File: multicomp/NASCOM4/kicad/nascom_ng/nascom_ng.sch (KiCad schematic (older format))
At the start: 20 parts, among them J1 Conn_02x14_Even_Odd, J14 Conn_02x08_Odd_Even, J2 Conn_02x14_Even_Odd, J3 Conn_02x14_Even_Odd, J4 Conn_02x14_Even_Odd, SW1 SW_Push, SW2 SW_Push, SW3 SW_Push

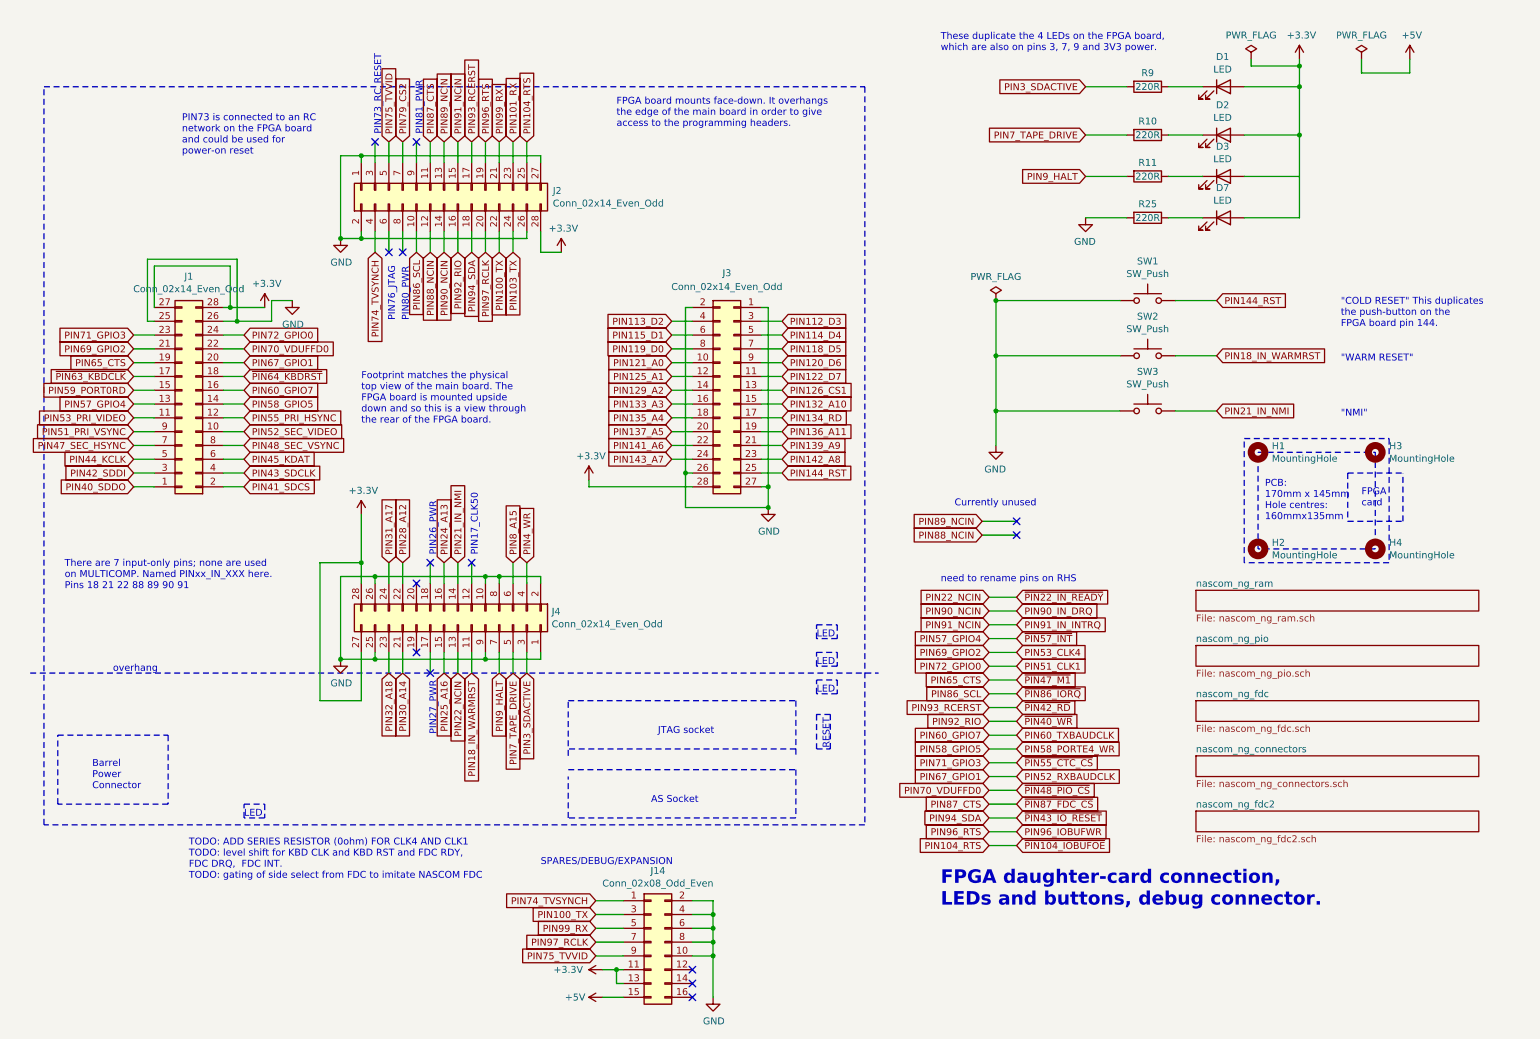
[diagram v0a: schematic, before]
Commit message: All nets routed, ref designators resequenced, nearly finished!
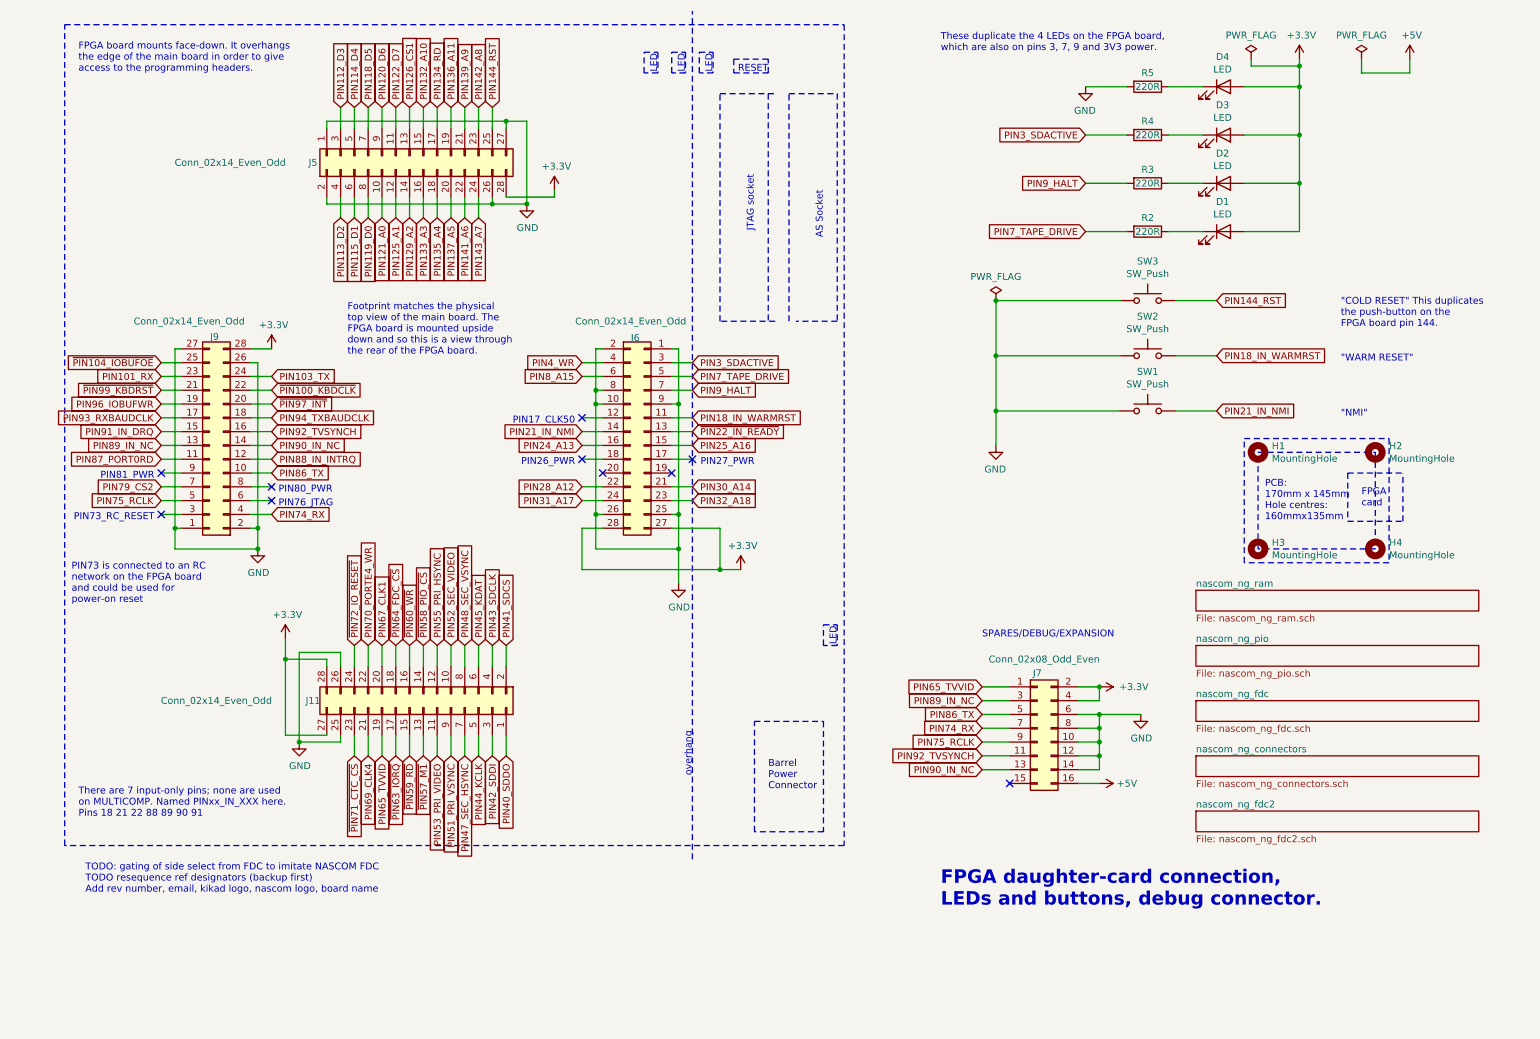
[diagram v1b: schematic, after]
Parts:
- renumbered D3 to D2, D2 to D3, D7 to D4, H3 to H2, H2 to H3, J1 to J11, J3 to J5, J4 to J6, J14 to J7, J2 to J9, R9 to R2, R11 to R3, R10 to R4, R25 to R5, SW3 to SW1, SW1 to SW3
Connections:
- net PIN89_NCIN is gone; now on net PIN89_IN_NC: J9.13 (Pin_13)
- net +3V3: now also J7.2 (Pin_2), J7.4 (Pin_4); no longer J7.11 (Pin_11), J7.13 (Pin_13)
- net +5V: now also J7.16 (Pin_16); no longer J7.15 (Pin_15)
- net GND: now also J7.12 (Pin_12), J7.14 (Pin_14); no longer J7.2 (Pin_2), J7.4 (Pin_4)
- net PIN3_SDACTIVE: now also R4.2; no longer R2.2
- net PIN7_TAPE_DRIVE: now also R2.2; no longer R4.2
- net PIN100_TX renamed PIN89_IN_NC
- net PIN89_IN_NC: no longer J9.22 (Pin_22)
- net PIN104_RTS renamed ~PIN104_IOBUFOE
- net PIN22_NCIN renamed ~PIN22_IN_READY
- net PIN51_CLK1 renamed ~PIN72_IO_RESET
- net PIN52_RXBAUDCLK renamed PIN67_CLK1
- net PIN53_CLK4 renamed PIN69_CLK4
- net PIN57_GPIO4 renamed ~PIN57_M1
- net PIN58_GPIO5 renamed ~PIN58_PIO_CS
- net PIN59_PORT0RD renamed ~PIN59_RD
- net PIN60_GPIO7 renamed ~PIN60_WR
- net PIN65_CTS renamed PIN65_TVVID
- net PIN65_TVVID: now also J7.1 (Pin_1)
- net PIN70_VDUFFD0 renamed PIN70_PORTE4_WR
- net PIN71_GPIO3 renamed ~PIN71_CTC_CS
- net PIN74_TVSYNCH renamed PIN74_RX
- net PIN74_RX: now also J7.7 (Pin_7); no longer J7.1 (Pin_1)
- net PIN75_TVVID renamed PIN75_RCLK
- net PIN86_SCL renamed PIN86_TX
- net PIN86_TX: now also J7.5 (Pin_5)
- net PIN87_CTS renamed PIN87_PORT0RD
- net PIN88_NCIN renamed PIN88_IN_INTRQ
- net PIN90_IN_DRQ renamed PIN90_IN_NC
- net PIN90_IN_NC: now also J7.13 (Pin_13)
- net PIN91_IN_INTRQ renamed PIN91_IN_DRQ
- net PIN92_RIO renamed PIN92_TVSYNCH
- net PIN92_TVSYNCH: now also J7.11 (Pin_11)
- net PIN93_RCERST renamed PIN93_RXBAUDCLK
- net PIN94_SDA renamed PIN94_TXBAUDCLK
- net PIN97_RCLK renamed ~PIN97_INT
- net ~PIN97_INT: no longer J7.7 (Pin_7)
- net PIN99_RX renamed ~PIN99_KBDRST
- net ~PIN99_KBDRST: no longer J7.5 (Pin_5)
- net ~PIN63_KBDCLK renamed ~PIN63_IORQ
- net ~PIN64_KBDRST renamed ~PIN64_FDC_CS
- new net ~PIN100_KBDCLK: J9.22 (Pin_22)
- no-connect marks 14 -> 10
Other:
- note added: "TODO: gating of side select from FDC to imitate NASCOM FDC\nTODO resequence ref designators (backup first)\nAdd rev number, email, kikad logo, nascom logo, board name"
- note removed: "Currently unused"
- note removed: "TODO: ADD SERIES RESISTOR (0ohm) FOR CLK4 AND CLK1\nTODO: level shift for KBD CLK and KBD RST and FDC RDY,\nFDC DRQ, FDC INT.\nTODO: gating of side select from FDC to imitate NASCOM FDC"
- note removed: "need to rename pins on RHS"
- moved on the sheet: D1, D2, D4, J11, J5, J6, J7, J9, R2, R3, R5

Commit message: Files for REV A release to PCB manufacture
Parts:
- added X1: NASCOM-logo, mylib:nascom_logo_tiny, symbol myLib:NASCOM-logo
- added X2: KiCad-sm-logo, mylib:KiCad-Logo_5mm_SolderMask, symbol myLib:KiCad-sm-logo
- renumbered J7 to J11, J5 to J6, J6 to J7, J9 to J8, J11 to J9, R5 to R1
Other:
- note added: "Barrel\nPower\nConnector\n(5V)"
- note added: "EP2C5T144C8N mini board\nmounts face-down. It overhangs\nthe edge of the main board in order to give\naccess to the programming headers."
- note added: "PCB setup:\nSet grid to 1.0mm for edge cuts and holes\nSet grid to 25mils for routing; tracks are\n0.25mm with 0.2mm spacing.\nChange IC pads to oval,\n1.6mm x 1.439mm to get 2 tracks through."
- note added: "TODO: gating of side select from FDC to imitate NASCOM FDC\n"
- note removed: "Barrel\nPower\nConnector"
- note removed: "FPGA board mounts face-down. It overhangs\nthe edge of the main board in order to give\naccess to the programming headers."
- note removed: "TODO: gating of side select from FDC to imitate NASCOM FDC\nTODO resequence ref designators (backup first)\nAdd rev number, email, kikad logo, nascom logo, board name"
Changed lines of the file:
@@
 Sheet 1 6
 Title "NASCOM 4 - a NASCOM in an FPGA"
-Date ""
-Rev "PRE-A"
+Date "14-Feb-2021"
+Rev "A"
 Comp ""
 Comment1 ""
@@
 PIN47_SEC_HSYNC
 $Comp
-L myLib:Conn_02x14_Even_Odd J5
+L myLib:Conn_02x14_Even_Odd J6
 U 1 1 5FEA6F67
 P 3300 1600
-F 0 "J5" V 3350 2300 50  0000 C CNN
+F 0 "J6" V 3350 2300 50  0000 C CNN
 F 1 "Conn_02x14_Even_Odd" V 3350 2900 50  0000 C CNN
 F 2 "Connector_PinSocket_2.54mm:PinSocket_2x14_P2.54mm_Vertical" H 3300 1600 50  0001 C CNN
@@
 PIN144_RST
 $Comp
-L myLib:Conn_02x14_Even_Odd J9
+L myLib:Conn_02x14_Even_Odd J8
 U 1 1 5FEAB151
 P 1950 3600
-F 0 "J9" H 2046 2812 50  0000 R CNN
+F 0 "J8" H 2046 2812 50  0000 R CNN
 F 1 "Conn_02x14_Even_Odd" H 2600 2700 50  0000 R CNN
 F 2 "Connector_PinSocket_2.54mm:PinSocket_2x14_P2.54mm_Vertical" H 1950 3600 50  0001 C CNN
@@
 	1650 4200 1600 4200
 $Comp
-L myLib:Conn_02x14_Even_Odd J6
+L myLib:Conn_02x14_Even_Odd J7
 U 1 1 5FEB71A3
 P 4900 3500
-F 0 "J6" H 4904 4180 50  0000 L CNN
+F 0 "J7" H 4904 4180 50  0000 L CNN
 F 1 "Conn_02x14_Even_Odd" H 4500 4300 50  0000 L CNN
 F 2 "Connector_PinSocket_2.54mm:PinSocket_2x14_P2.54mm_Vertical" H 4900 3500 50  0001 C CNN
@@
 Text Notes 5800 2050 1    50   ~ 0
 JTAG socket\n
-Text Notes 5900 6100 0    50   ~ 0
-Barrel\nPower\nConnector
+Text Notes 5850 6150 0    50   ~ 0
+Barrel\nPower\nConnector\n(5V)
 $Comp
 L Device:LED D1
@@
 	7450 5850 7650 5850
 Text Notes 950  6850 0    50   ~ 0
-TODO: gating of side select from FDC to imitate NASCOM FDC\nTODO resequence ref designators (backup first)\nAdd rev number, email, kikad logo, nascom logo, board name
+TODO: gating of side select from FDC to imitate NASCOM FDC\n
 Text Notes 4500 3450 2    50   ~ 0
 PIN17_CLK50
@@
 $EndComp
 $Comp
-L Device:R R5
+L Device:R R1
 U 1 1 6000B7FC
 P 8650 1000
-F 0 "R5" V 8550 1000 50  0000 C CNN
+F 0 "R1" V 8550 1000 50  0000 C CNN
 F 1 "220R" V 8650 1000 50  0000 C CNN
 F 2 "Resistor_THT:R_Axial_DIN0204_L3.6mm_D1.6mm_P7.62mm_Horizontal" V 8580 1000 50  0001 C CNN
@@
 Text Notes 850  4750 0    50   ~ 0
 PIN73 is connected to an RC\nnetwork on the FPGA board\nand could be used for\npower-on reset
-Text Notes 900  900  0    50   ~ 0
-FPGA board mounts face-down. It overhangs\nthe edge of the main board in order to give\naccess to the programming headers.
+Text Notes 900  950  0    50   ~ 0
+EP2C5T144C8N mini board\nmounts face-down. It overhangs\nthe edge of the main board in order to give\naccess to the programming headers.
 Wire Notes Line
 	5350 6600 5350 450
@@
 AR Path="/5FC877BB/601658F1" Ref="PL?"  Part="1"
 AR Path="/5FC85C78/601658F1" Ref="PL?"  Part="1"
-AR Path="/601658F1" Ref="J7"  Part="1"
-F 0 "J7" H 7850 6050 50  0000 C CNN
+AR Path="/601658F1" Ref="J11"  Part="1"
+F 0 "J11" H 7850 6050 50  0000 C CNN
 F 1 "Conn_02x08_Odd_Even" H 7900 6150 50  0000 C CNN
 F 2 "Connector_IDC:IDC-Header_2x08_P2.54mm_Vertical" H 7850 5650 50  0001 C CNN
@@
 Connection ~ 2500 5750
 $Comp
-L myLib:Conn_02x14_Even_Odd J11
+L myLib:Conn_02x14_Even_Odd J9
 U 1 1 5FE8AA27
 P 3400 5400
-F 0 "J11" V 3450 4600 50  0000 C CNN
+F 0 "J9" V 3450 4600 50  0000 C CNN
 F 1 "Conn_02x14_Even_Odd" V 3450 3900 50  0000 C CNN
 F 2 "Connector_PinSocket_2.54mm:PinSocket_2x14_P2.54mm_Vertical" H 3400 5400 50  0001 C CNN
@@
 	9750 1700 9750 2050
 Connection ~ 9750 1700
+$Comp
+L myLib:NASCOM-logo X1
+U 1 1 602D8669
+P 8450 4100
+F 0 "X1" H 8150 4200 50  0000 C CNN
+F 1 "NASCOM-logo" H 8750 4200 50  0000 C CNN
+F 2 "mylib:nascom_logo_tiny" H 8450 4100 50  0001 C CNN
+F 3 "" H 8450 4100 50  0001 C CNN
+	1    8450 4100
+	1    0    0    -1
+$EndComp
+$Comp
+L myLib:KiCad-sm-logo X2
+U 1 1 602EF72E
+P 8450 4300
+F 0 "X2" H 8150 4400 50  0000 C CNN
+F 1 "KiCad-sm-logo" H 8800 4400 50  0000 C CNN
+F 2 "mylib:KiCad-Logo_5mm_SolderMask" H 8450 4300 50  0001 C CNN
+F 3 "" H 8450 4300 50  0001 C CNN
+	1    8450 4300
+	1    0    0    -1
+$EndComp
+Text Notes 850  7650 0    50   ~ 0
+PCB setup:\nSet grid to 1.0mm for edge cuts and holes\nSet grid to 25mils for routing; tracks are\n0.25mm with 0.2mm spacing.\nChange IC pads to oval,\n1.6mm x 1.439mm to get 2 tracks through.
 $EndSCHEMATC
